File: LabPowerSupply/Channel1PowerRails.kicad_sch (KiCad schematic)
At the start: 8 parts

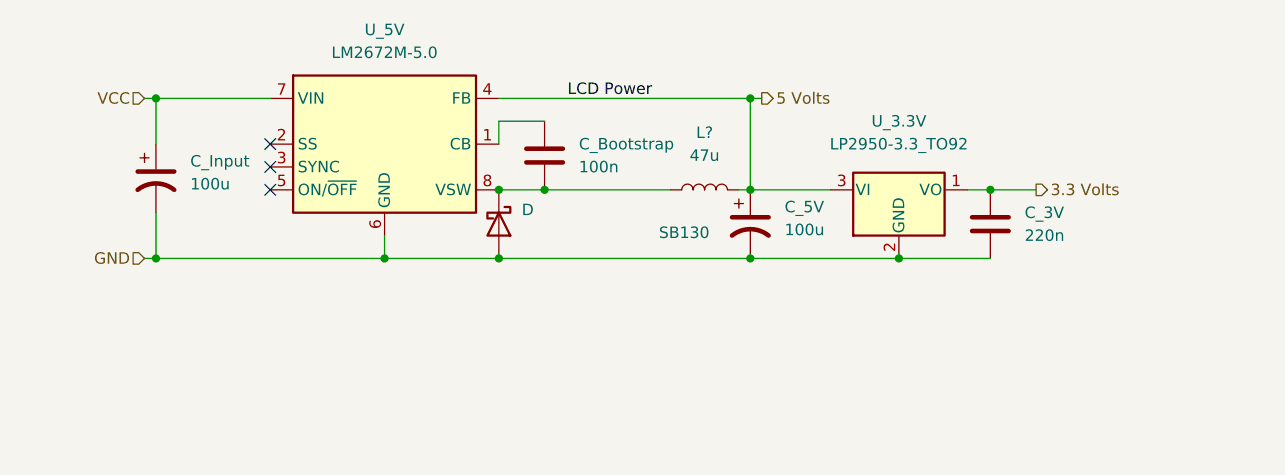
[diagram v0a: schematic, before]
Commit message: Finished first pass on the schematic
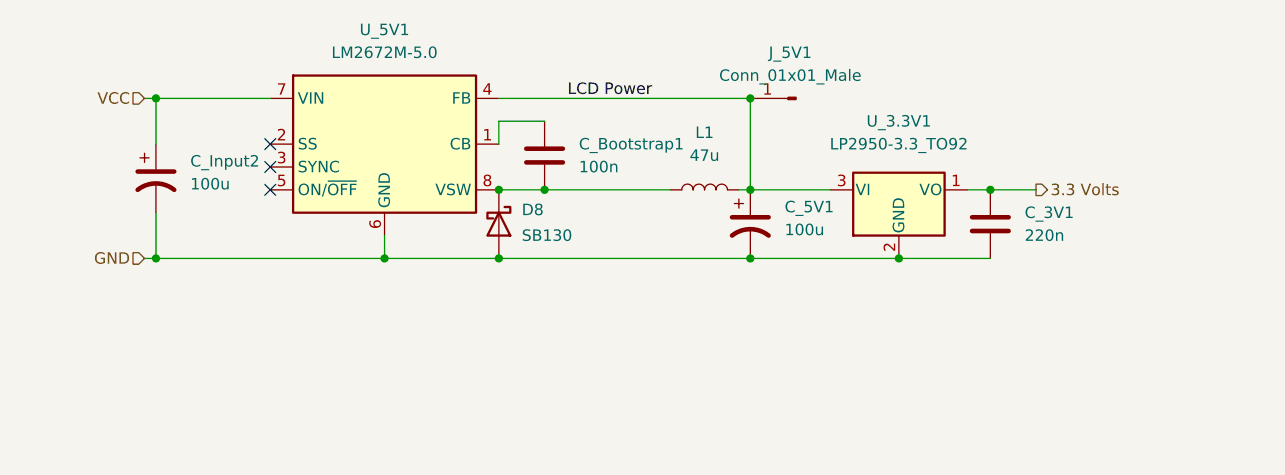
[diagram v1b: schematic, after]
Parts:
- added J_5V1: Conn_01x01_Male, Connector_PinHeader_2.54mm:PinHeader_1x01_P2.54mm_Vertical, symbol Connector:Conn_01x01_Male
- gave numbers to parts that had none: 1
- renumbered C_3V to C_3V1, C_5V to C_5V1, C_Bootstrap to C_Bootstrap1, C_Input to C_Input2, D to D8, U_3.3V to U_3.3V1, U_5V to U_5V1
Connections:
- net 5 Volts renamed LCD Power
- net LCD Power: now also J_5V1.1 (Pin_1)
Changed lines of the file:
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@@
   (junction (at 139.7 106.68) (diameter 0) (color 0 0 0 0)
   )
+  (junction (at 144.78 99.06) (diameter 0) (color 0 0 0 0)
+  )
+  (junction (at 167.64 99.06) (diameter 0) (color 0 0 0 0)
+  )
   (junction (at 167.64 88.9) (diameter 0) (color 0 0 0 0)
-  )
-  (junction (at 144.78 99.06) (diameter 0) (color 0 0 0 0)
-  )
-  (junction (at 167.64 99.06) (diameter 0) (color 0 0 0 0)
   )
   (junction (at 101.6 106.68) (diameter 0) (color 0 0 0 0)
@@
     (stroke (width 0) (type default) (color 0 0 0 0))
   )
-  (wire (pts (xy 167.64 88.9) (xy 168.91 88.9))
-    (stroke (width 0) (type default) (color 0 0 0 0))
-  )
   (wire (pts (xy 139.7 106.68) (xy 167.64 106.68))
     (stroke (width 0) (type default) (color 0 0 0 0))
@@
     (effects (font (size 1.27 1.27)) (justify left bottom))
   )
-  (hierarchical_label "5 Volts" (shape output) (at 168.91 88.9 0)
-    (effects (font (size 1.27 1.27)) (justify left))
-  )
   (hierarchical_label "GND" (shape input) (at 100.33 106.68 180)
     (effects (font (size 1.27 1.27)) (justify right))
@@
     (effects (font (size 1.27 1.27)) (justify right))
   )
+  (symbol (lib_id "Connector:Conn_01x01_Male") (at 172.72 88.9 180) (unit 1)
+    (in_bom yes) (on_board yes) (fields_autoplaced)
+    (property "Reference" "J_5V1" (id 0) (at 172.085 83.82 0))
+    (property "Value" "Conn_01x01_Male" (id 1) (at 172.085 86.36 0))
+    (property "Footprint" "Connector_PinHeader_2.54mm:PinHeader_1x01_P2.54mm_Vertical" (id 2) (at 172.72 88.9 0)
+      (effects (font (size 1.27 1.27)) hide)
+    )
+    (property "Datasheet" "~" (id 3) (at 172.72 88.9 0)
+      (effects (font (size 1.27 1.27)) hide)
+    )
+    (pin "1")
+  )
   (symbol (lib_id "Device:C") (at 194.31 102.87 0) (unit 1)
     (in_bom yes) (on_board yes) (fields_autoplaced)
-    (property "Reference" "C_3V" (id 0) (at 198.12 101.5999 0)
+    (property "Reference" "C_3V1" (id 0) (at 198.12 101.5999 0)
       (effects (font (size 1.27 1.27)) (justify left))
     )
@@
   (symbol (lib_id "Regulator_Linear:LP2950-3.3_TO92") (at 184.15 99.06 0) (unit 1)
     (in_bom yes) (on_board yes) (fields_autoplaced)
-    (property "Reference" "U_3.3V" (id 0) (at 184.15 91.44 0))
+    (property "Reference" "U_3.3V1" (id 0) (at 184.15 91.44 0))
     (property "Value" "LP2950-3.3_TO92" (id 1) (at 184.15 93.98 0))
     (property "Footprint" "Package_TO_SOT_THT:TO-92_Inline" (id 2) (at 184.15 93.345 0)
@@
   (symbol (lib_id "Device:C_Polarized_US") (at 167.64 102.87 0) (unit 1)
     (in_bom yes) (on_board yes) (fields_autoplaced)
-    (property "Reference" "C_5V" (id 0) (at 171.45 100.9649 0)
+    (property "Reference" "C_5V1" (id 0) (at 171.45 100.9649 0)
       (effects (font (size 1.27 1.27)) (justify left))
     )
@@
   (symbol (lib_id "Diode:SB130") (at 139.7 102.87 270) (unit 1)
     (in_bom yes) (on_board yes)
-    (property "Reference" "D" (id 0) (at 142.24 101.2824 90)
-      (effects (font (size 1.27 1.27)) (justify left))
-    )
-    (property "Value" "SB130" (id 1) (at 157.48 103.8224 90)
+    (property "Reference" "D8" (id 0) (at 142.24 101.2824 90)
+      (effects (font (size 1.27 1.27)) (justify left))
+    )
+    (property "Value" "SB130" (id 1) (at 142.24 104.14 90)
       (effects (font (size 1.27 1.27)) (justify left))
     )
@@
   (symbol (lib_id "Device:L") (at 162.56 99.06 90) (unit 1)
     (in_bom yes) (on_board yes) (fields_autoplaced)
-    (property "Reference" "L?" (id 0) (at 162.56 92.71 90))
+    (property "Reference" "L1" (id 0) (at 162.56 92.71 90))
     (property "Value" "47u" (id 1) (at 162.56 95.25 90))
     (property "Footprint" "Inductor_SMD:L_1210_3225Metric" (id 2) (at 162.56 99.06 0)
@@
   (symbol (lib_id "Regulator_Switching:LM2672M-5.0") (at 127 93.98 0) (unit 1)
     (in_bom yes) (on_board yes) (fields_autoplaced)
-    (property "Reference" "U_5V" (id 0) (at 127 81.28 0))
+    (property "Reference" "U_5V1" (id 0) (at 127 81.28 0))
     (property "Value" "LM2672M-5.0" (id 1) (at 127 83.82 0))
     (property "Footprint" "Package_SO:SOIC-8_3.9x4.9mm_P1.27mm" (id 2) (at 128.27 102.87 0)
@@
   (symbol (lib_id "Device:C_Polarized_US") (at 101.6 97.79 0) (unit 1)
     (in_bom yes) (on_board yes) (fields_autoplaced)
-    (property "Reference" "C_Input" (id 0) (at 105.41 95.8849 0)
+    (property "Reference" "C_Input2" (id 0) (at 105.41 95.8849 0)
       (effects (font (size 1.27 1.27)) (justify left))
     )
@@
   (symbol (lib_id "Device:C") (at 144.78 95.25 0) (unit 1)
     (in_bom yes) (on_board yes) (fields_autoplaced)
-    (property "Reference" "C_Bootstrap" (id 0) (at 148.59 93.9799 0)
-      (effects (font (size 1.27 1.27)) (justify left))
-    )
+    (property "Reference" "C_Bootstrap1" (id 0) (at 148.59 93.9799 0)
+      (effects (font (size 1.27 1.27)) (justify left))
+    )

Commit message: started PCB
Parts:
- removed C_Input2: 100u, Capacitor_THT:CP_Radial_D12.5mm_P5.00mm, symbol Device:C_Polarized_US
- C_5V1: footprint Capacitor_THT:CP_Radial_D12.5mm_P5.00mm -> Capacitor_THT:CP_Radial_D10.0mm_P5.00mm
- L1: footprint Inductor_SMD:L_1210_3225Metric -> Inductor_THT:L_Radial_D6.0mm_P4.00mm
- renumbered U_3.3V1 to U_3.3V2
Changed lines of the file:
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@@
     (rev "1")
     (company "George Mason University")
+    (comment 1 "powered off the 3.3 volt rail.")
+    (comment 2 "display as it requires it. The rest of the perphierals and the MCU are")
+    (comment 3 "side. The 5 volts rail is only used to power the 20x04 character LCD")
+    (comment 4 "This supplys the 5 volts and 3.3 volts rail for the primary digital")
   )
   (junction (at 127 106.68) (diameter 0) (color 0 0 0 0)
@@
   (junction (at 167.64 88.9) (diameter 0) (color 0 0 0 0)
   )
-  (junction (at 101.6 106.68) (diameter 0) (color 0 0 0 0)
-  )
   (junction (at 194.31 99.06) (diameter 0) (color 0 0 0 0)
   )
   (junction (at 167.64 106.68) (diameter 0) (color 0 0 0 0)
-  )
-  (junction (at 101.6 88.9) (diameter 0) (color 0 0 0 0)
   )
   (junction (at 184.15 106.68) (diameter 0) (color 0 0 0 0)
@@
     (stroke (width 0) (type default) (color 0 0 0 0))
   )
-  (wire (pts (xy 100.33 88.9) (xy 101.6 88.9))
+  (wire (pts (xy 113.03 88.9) (xy 114.3 88.9))
     (stroke (width 0) (type default) (color 0 0 0 0))
   )
@@
     (stroke (width 0) (type default) (color 0 0 0 0))
   )
-  (wire (pts (xy 101.6 106.68) (xy 127 106.68))
-    (stroke (width 0) (type default) (color 0 0 0 0))
-  )
-  (wire (pts (xy 101.6 101.6) (xy 101.6 106.68))
-    (stroke (width 0) (type default) (color 0 0 0 0))
-  )
   (wire (pts (xy 144.78 91.44) (xy 139.7 91.44))
     (stroke (width 0) (type default) (color 0 0 0 0))
@@
     (stroke (width 0) (type default) (color 0 0 0 0))
   )
-  (wire (pts (xy 101.6 88.9) (xy 114.3 88.9))
-    (stroke (width 0) (type default) (color 0 0 0 0))
-  )
   (wire (pts (xy 139.7 106.68) (xy 167.64 106.68))
     (stroke (width 0) (type default) (color 0 0 0 0))
   )
-  (wire (pts (xy 100.33 106.68) (xy 101.6 106.68))
+  (wire (pts (xy 113.03 106.68) (xy 127 106.68))
     (stroke (width 0) (type default) (color 0 0 0 0))
   )
@@
   )
   (wire (pts (xy 166.37 99.06) (xy 167.64 99.06))
-    (stroke (width 0) (type default) (color 0 0 0 0))
-  )
-  (wire (pts (xy 101.6 88.9) (xy 101.6 93.98))
     (stroke (width 0) (type default) (color 0 0 0 0))
   )
@@
     (effects (font (size 1.27 1.27)) (justify left bottom))
   )
-  (hierarchical_label "GND" (shape input) (at 100.33 106.68 180)
+  (hierarchical_label "GND" (shape input) (at 113.03 106.68 180)
     (effects (font (size 1.27 1.27)) (justify right))
   )
@@
     (effects (font (size 1.27 1.27)) (justify left))
   )
-  (hierarchical_label "VCC" (shape input) (at 100.33 88.9 180)
+  (hierarchical_label "VCC" (shape input) (at 113.03 88.9 180)
     (effects (font (size 1.27 1.27)) (justify right))
   )
@@
   (symbol (lib_id "Regulator_Linear:LP2950-3.3_TO92") (at 184.15 99.06 0) (unit 1)
     (in_bom yes) (on_board yes) (fields_autoplaced)
-    (property "Reference" "U_3.3V1" (id 0) (at 184.15 91.44 0))
+    (property "Reference" "U_3.3V2" (id 0) (at 184.15 91.44 0))
     (property "Value" "LP2950-3.3_TO92" (id 1) (at 184.15 93.98 0))
     (property "Footprint" "Package_TO_SOT_THT:TO-92_Inline" (id 2) (at 184.15 93.345 0)
@@
       (effects (font (size 1.27 1.27)) (justify left))
     )
-    (property "Footprint" "Capacitor_THT:CP_Radial_D12.5mm_P5.00mm" (id 2) (at 167.64 102.87 0)
+    (property "Footprint" "Capacitor_THT:CP_Radial_D10.0mm_P5.00mm" (id 2) (at 167.64 102.87 0)
       (effects (font (size 1.27 1.27)) hide)
     )
@@
     (property "Reference" "L1" (id 0) (at 162.56 92.71 90))
     (property "Value" "47u" (id 1) (at 162.56 95.25 90))
-    (property "Footprint" "Inductor_SMD:L_1210_3225Metric" (id 2) (at 162.56 99.06 0)
+    (property "Footprint" "Inductor_THT:L_Radial_D6.0mm_P4.00mm" (id 2) (at 162.56 99.06 0)
       (effects (font (size 1.27 1.27)) hide)
     )
@@
     (pin "8")
   )
-  (symbol (lib_id "Device:C_Polarized_US") (at 101.6 97.79 0) (unit 1)
-    (in_bom yes) (on_board yes) (fields_autoplaced)
-    (property "Reference" "C_Input2" (id 0) (at 105.41 95.8849 0)
-      (effects (font (size 1.27 1.27)) (justify left))
-    )
-    (property "Value" "100u" (id 1) (at 105.41 98.4249 0)
-      (effects (font (size 1.27 1.27)) (justify left))
-    )
-    (property "Footprint" "Capacitor_THT:CP_Radial_D12.5mm_P5.00mm" (id 2) (at 101.6 97.79 0)
-      (effects (font (size 1.27 1.27)) hide)
-    )
-    (property "Datasheet" "~" (id 3) (at 101.6 97.79 0)
-      (effects (font (size 1.27 1.27)) hide)
-    )
-    (pin "1")
-    (pin "2")
-  )
   (symbol (lib_id "Device:C") (at 144.78 95.25 0) (unit 1)

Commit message: more work
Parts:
- renumbered C_Bootstrap1 to C1_5V1, C_5V1 to C2_5V1, D8 to D_5V1, L1 to L_5V1, U_3.3V2 to U_3.3V1
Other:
- moved on the sheet: L_5V1
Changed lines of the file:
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@@
     (stroke (width 0) (type default) (color 0 0 0 0))
   )
-  (wire (pts (xy 158.75 99.06) (xy 144.78 99.06))
+  (wire (pts (xy 156.21 99.06) (xy 144.78 99.06))
     (stroke (width 0) (type default) (color 0 0 0 0))
   )
@@
     (stroke (width 0) (type default) (color 0 0 0 0))
   )
-  (wire (pts (xy 166.37 99.06) (xy 167.64 99.06))
+  (wire (pts (xy 163.83 99.06) (xy 167.64 99.06))
     (stroke (width 0) (type default) (color 0 0 0 0))
   )
@@
   (symbol (lib_id "Regulator_Linear:LP2950-3.3_TO92") (at 184.15 99.06 0) (unit 1)
     (in_bom yes) (on_board yes) (fields_autoplaced)
-    (property "Reference" "U_3.3V2" (id 0) (at 184.15 91.44 0))
+    (property "Reference" "U_3.3V1" (id 0) (at 184.15 91.44 0))
     (property "Value" "LP2950-3.3_TO92" (id 1) (at 184.15 93.98 0))
     (property "Footprint" "Package_TO_SOT_THT:TO-92_Inline" (id 2) (at 184.15 93.345 0)
@@
   (symbol (lib_id "Device:C_Polarized_US") (at 167.64 102.87 0) (unit 1)
     (in_bom yes) (on_board yes) (fields_autoplaced)
-    (property "Reference" "C_5V1" (id 0) (at 171.45 100.9649 0)
+    (property "Reference" "C2_5V1" (id 0) (at 171.45 100.9649 0)
       (effects (font (size 1.27 1.27)) (justify left))
     )
@@
   (symbol (lib_id "Diode:SB130") (at 139.7 102.87 270) (unit 1)
     (in_bom yes) (on_board yes)
-    (property "Reference" "D8" (id 0) (at 142.24 101.2824 90)
+    (property "Reference" "D_5V1" (id 0) (at 142.24 101.2824 90)
       (effects (font (size 1.27 1.27)) (justify left))
     )
@@
     (pin "2")
   )
-  (symbol (lib_id "Device:L") (at 162.56 99.06 90) (unit 1)
+  (symbol (lib_id "Device:L") (at 160.02 99.06 90) (unit 1)
     (in_bom yes) (on_board yes) (fields_autoplaced)
-    (property "Reference" "L1" (id 0) (at 162.56 92.71 90))
-    (property "Value" "47u" (id 1) (at 162.56 95.25 90))
-    (property "Footprint" "Inductor_THT:L_Radial_D6.0mm_P4.00mm" (id 2) (at 162.56 99.06 0)
+    (property "Reference" "L_5V1" (id 0) (at 160.02 92.71 90))
+    (property "Value" "47u" (id 1) (at 160.02 95.25 90))
+    (property "Footprint" "Inductor_THT:L_Radial_D6.0mm_P4.00mm" (id 2) (at 160.02 99.06 0)
       (effects (font (size 1.27 1.27)) hide)
     )
-    (property "Datasheet" "~" (id 3) (at 162.56 99.06 0)
+    (property "Datasheet" "~" (id 3) (at 160.02 99.06 0)
       (effects (font (size 1.27 1.27)) hide)
     )
@@
   (symbol (lib_id "Device:C") (at 144.78 95.25 0) (unit 1)
     (in_bom yes) (on_board yes) (fields_autoplaced)
-    (property "Reference" "C_Bootstrap1" (id 0) (at 148.59 93.9799 0)
+    (property "Reference" "C1_5V1" (id 0) (at 148.59 93.9799 0)
       (effects (font (size 1.27 1.27)) (justify left))
     )

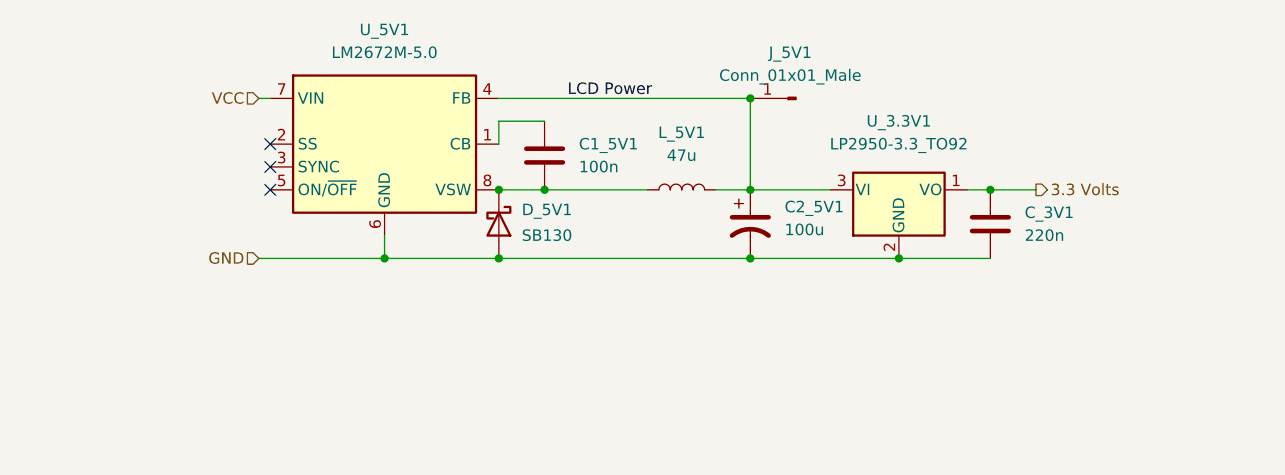
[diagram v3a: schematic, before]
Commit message: Resistor footprints changed to 0603
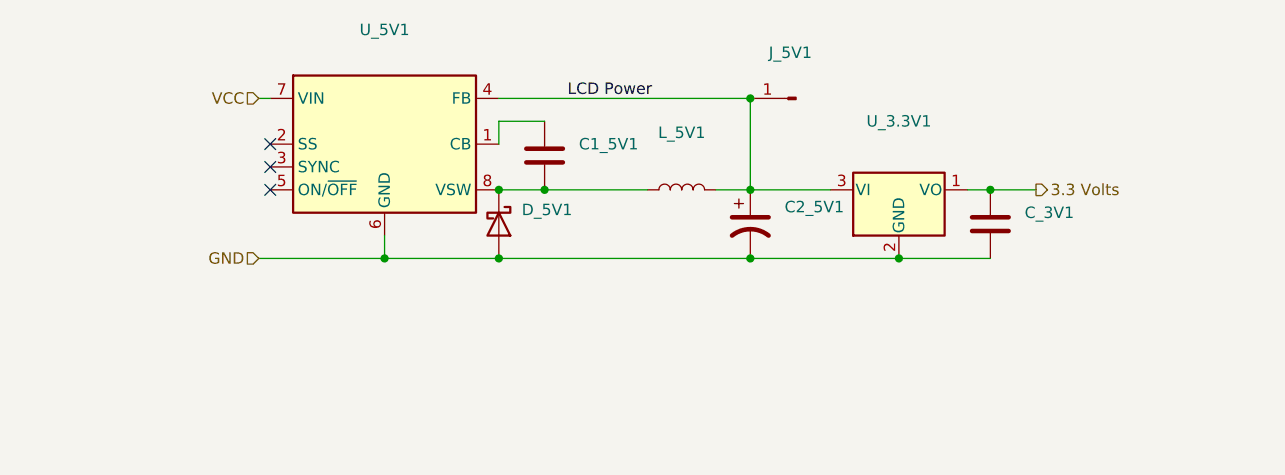
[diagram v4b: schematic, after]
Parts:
- C1_5V1: value 100n -> (none); footprint Capacitor_SMD:C_1210_3225Metric -> (none)
- C2_5V1: value 100u -> (none); footprint Capacitor_THT:CP_Radial_D10.0mm_P5.00mm -> (none)
- C_3V1: value 220n -> (none); footprint Capacitor_SMD:C_1210_3225Metric -> (none)
- D_5V1: value SB130 -> (none); footprint Diode_THT:D_DO-41_SOD81_P10.16mm_Horizontal -> (none)
- J_5V1: value Conn_01x01_Male -> (none); footprint Connector_PinHeader_2.54mm:PinHeader_1x01_P2.54mm_Vertical -> (none)
- L_5V1: value 47u -> (none); footprint Inductor_THT:L_Radial_D6.0mm_P4.00mm -> (none)
- U_3.3V1: value LP2950-3.3_TO92 -> (none); footprint Package_TO_SOT_THT:TO-92_Inline -> (none)
- U_5V1: value LM2672M-5.0 -> (none); footprint Package_SO:SOIC-8_3.9x4.9mm_P1.27mm -> (none)
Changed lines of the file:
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@@
     (in_bom yes) (on_board yes) (fields_autoplaced)
     (property "Reference" "J_5V1" (id 0) (at 172.085 83.82 0))
-    (property "Value" "Conn_01x01_Male" (id 1) (at 172.085 86.36 0))
-    (property "Footprint" "Connector_PinHeader_2.54mm:PinHeader_1x01_P2.54mm_Vertical" (id 2) (at 172.72 88.9 0)
+    (property "Value" "" (id 1) (at 172.085 86.36 0))
+    (property "Footprint" "" (id 2) (at 172.72 88.9 0)
       (effects (font (size 1.27 1.27)) hide)
     )
@@
       (effects (font (size 1.27 1.27)) (justify left))
     )
-    (property "Value" "220n" (id 1) (at 198.12 104.1399 0)
+    (property "Value" "" (id 1) (at 198.12 104.1399 0)
       (effects (font (size 1.27 1.27)) (justify left))
     )
-    (property "Footprint" "Capacitor_SMD:C_1210_3225Metric" (id 2) (at 195.2752 106.68 0)
+    (property "Footprint" "" (id 2) (at 195.2752 106.68 0)
       (effects (font (size 1.27 1.27)) hide)
     )
@@
     (in_bom yes) (on_board yes) (fields_autoplaced)
     (property "Reference" "U_3.3V1" (id 0) (at 184.15 91.44 0))
-    (property "Value" "LP2950-3.3_TO92" (id 1) (at 184.15 93.98 0))
-    (property "Footprint" "Package_TO_SOT_THT:TO-92_Inline" (id 2) (at 184.15 93.345 0)
+    (property "Value" "" (id 1) (at 184.15 93.98 0))
+    (property "Footprint" "" (id 2) (at 184.15 93.345 0)
       (effects (font (size 1.27 1.27) italic) hide)
     )
@@
       (effects (font (size 1.27 1.27)) (justify left))
     )
-    (property "Value" "100u" (id 1) (at 171.45 103.5049 0)
+    (property "Value" "" (id 1) (at 171.45 103.5049 0)
       (effects (font (size 1.27 1.27)) (justify left))
     )
-    (property "Footprint" "Capacitor_THT:CP_Radial_D10.0mm_P5.00mm" (id 2) (at 167.64 102.87 0)
+    (property "Footprint" "" (id 2) (at 167.64 102.87 0)
       (effects (font (size 1.27 1.27)) hide)
     )
@@
       (effects (font (size 1.27 1.27)) (justify left))
     )
-    (property "Value" "SB130" (id 1) (at 142.24 104.14 90)
+    (property "Value" "" (id 1) (at 142.24 104.14 90)
       (effects (font (size 1.27 1.27)) (justify left))
     )
-    (property "Footprint" "Diode_THT:D_DO-41_SOD81_P10.16mm_Horizontal" (id 2) (at 135.255 102.87 0)
+    (property "Footprint" "" (id 2) (at 135.255 102.87 0)
       (effects (font (size 1.27 1.27)) hide)
     )
@@
     (in_bom yes) (on_board yes) (fields_autoplaced)
     (property "Reference" "L_5V1" (id 0) (at 160.02 92.71 90))
-    (property "Value" "47u" (id 1) (at 160.02 95.25 90))
-    (property "Footprint" "Inductor_THT:L_Radial_D6.0mm_P4.00mm" (id 2) (at 160.02 99.06 0)
+    (property "Value" "" (id 1) (at 160.02 95.25 90))
+    (property "Footprint" "" (id 2) (at 160.02 99.06 0)
       (effects (font (size 1.27 1.27)) hide)
     )
@@
     (in_bom yes) (on_board yes) (fields_autoplaced)
     (property "Reference" "U_5V1" (id 0) (at 127 81.28 0))
-    (property "Value" "LM2672M-5.0" (id 1) (at 127 83.82 0))
-    (property "Footprint" "Package_SO:SOIC-8_3.9x4.9mm_P1.27mm" (id 2) (at 128.27 102.87 0)
+    (property "Value" "" (id 1) (at 127 83.82 0))
+    (property "Footprint" "" (id 2) (at 128.27 102.87 0)
       (effects (font (size 1.27 1.27) italic) (justify left) hide)
     )
@@
       (effects (font (size 1.27 1.27)) (justify left))
     )
-    (property "Value" "100n" (id 1) (at 148.59 96.5199 0)
+    (property "Value" "" (id 1) (at 148.59 96.5199 0)
       (effects (font (size 1.27 1.27)) (justify left))
     )
-    (property "Footprint" "Capacitor_SMD:C_1210_3225Metric" (id 2) (at 145.7452 99.06 0)
+    (property "Footprint" "" (id 2) (at 145.7452 99.06 0)
       (effects (font (size 1.27 1.27)) hide)
     )
